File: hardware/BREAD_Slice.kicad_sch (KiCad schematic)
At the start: 15 parts, among them J1 Conn_01x10_Female, J2 I2C_01x04

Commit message: Initial commit
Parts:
- removed C1, C3, C4: 22uF, Capacitor_SMD:C_1206_3216Metric, symbol Device:C_Small
- removed C2: 100nF, Capacitor_SMD:C_1206_3216Metric, symbol Device:C_Small
- removed D1: WS2812B_5050, SparkFun-LED:WS2812-5050-4PIN, symbol SparkFun-LED:WS2812B_5050
- removed HS1: Heatsink_Pad, SparkFun-Fuse:Thermal Pad, symbol Mechanical:Heatsink_Pad
- removed J2: I2C_01x04, Connector_JST:JST_SH_SM04B-SRSS-TB_1x04-1MP_P1.00mm_Horizontal, symbol SparkFun-Connector:I2C_01x04
- removed L1: 4.7uH, Inductor_SMD:L_1210_3225Metric, symbol Device:L_Small
- removed U1: ~, Package_TO_SOT_SMD:TSOT-23-6, symbol SparkFun-DiscreteSemi:AP63205
- added C1, C2: 10uF_t, OCI_UPL_FOOTPRINTS:C_2312, symbol BREAD_Slice-rescue:10uF_t-OCI_UPL_2_Capacitors
- added D1, D2, D3, D4: D, Diode_SMD:D_1206_3216Metric_Pad1.42x1.75mm_HandSolder, symbol Device:D
- added D5, D6, D7, D8: D_Zener, Diode_SMD:D_1206_3216Metric_Pad1.42x1.75mm_HandSolder, symbol Device:D_Zener
- added J2, J3, J4, J5: Screw_Terminal_01x03, TerminalBlock_TE-Connectivity:TerminalBlock_TE_282834-3_1x03_P2.54mm_Horizontal, symbol Connector:Screw_Terminal_01x03
- added J6: Screw_Terminal_01x04, TerminalBlock_TE-Connectivity:TerminalBlock_TE_282834-4_1x04_P2.54mm_Horizontal, symbol Connector:Screw_Terminal_01x04
- added K1, K2, K3, K4: G5Q-1, Relay_THT:Relay_SPDT_Omron-G5Q-1, symbol Relay:G5Q-1
- added Logo1: Logo_Open_Hardware_Small, Symbol:OSHW-Symbol_6.7x6mm_SilkScreen, symbol Graphic:Logo_Open_Hardware_Small
- added R1, R2, R3, R4: 1k, Resistor_SMD:R_1206_3216Metric_Pad1.30x1.75mm_HandSolder, symbol BREAD_Slice-rescue:R-OCI_UPL_1_Resistors
- added RV1, RV2, RV3, RV4: 10k, Potentiometer_THT:Potentiometer_Bourns_3266W_Vertical, symbol BREAD_Slice-rescue:R_POT_TRIM-Device
- added U1, U2, U3, U4: TCMT1100, Package_SO:SOP-4_4.4x2.6mm_P1.27mm, symbol Isolator:TCMT1100
- H1, H4: footprint MountingHole:MountingHole_5mm -> MountingHole:MountingHole_3.2mm_M3_DIN965_Pad
- H2: renamed from H3; footprint MountingHole:MountingHole_5mm -> MountingHole:MountingHole_3.2mm_M3_DIN965_Pad
- H3: renamed from H2; footprint MountingHole:MountingHole_5mm -> MountingHole:MountingHole_3.2mm_M3_DIN965_Pad
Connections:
- net +12V: now also A1.30 (VIN), C1.1
- net +5V: now also C2.1, D1.1 (K), D2.1 (K), D3.1 (K), D4.1 (K), K1.5, K2.5, K3.5, K4.5
- net GND: now also C1.2, C2.2, D5.1 (K), D5.2 (A), D6.1 (K), D6.2 (A), D7.1 (K), D7.2 (A), D8.1 (K), D8.2 (A), RV1.3, RV2.3, RV3.3, RV4.3, U1.2, U1.3, U2.2, U2.3, U3.2, U3.3, U4.2, U4.3
- net SW2: now reaches A1.12 (D9)
- net SW2: now also R3.1
- net SW3: now reaches A1.13 (D10)
- net SW3: now also R2.1
- net SW4: now reaches A1.14 (D11)
- net SW4: now also R4.1
- net A_IN1: now reaches A1.19 (A0)
- net A_IN1: now also RV1.2
- net A_IN2: now reaches A1.20 (A1)
- net A_IN2: now also RV2.2
- net A_IN3: now reaches A1.21 (A2)
- net A_IN3: now also RV3.2
- net A_IN4: now reaches A1.22 (A3)
- net A_IN4: now also RV4.2
- net SW1: now reaches A1.9 (D6)
- net SW1: now also R1.1
- net LED: no longer names the net of A1.8 (D5)
- new net: D1.2 (A), K1.1, U1.4
- new net: R1.2, U1.1
- new net: J2.1 (Pin_1), K1.4
- new net: J2.2 (Pin_2), K1.3
- new net: J2.3 (Pin_3), K1.2
- new net: D2.2 (A), K3.1, U2.4
- new net: R2.2, U2.1
- new net: J3.1 (Pin_1), K3.4
- new net: J3.2 (Pin_2), K3.3
- new net: J3.3 (Pin_3), K3.2
- new net: D3.2 (A), K2.1, U3.4
- new net: R3.2, U3.1
- new net: J4.1 (Pin_1), K2.4
- new net: J4.2 (Pin_2), K2.3
- new net: J4.3 (Pin_3), K2.2
- new net: D4.2 (A), K4.1, U4.4
- new net: R4.2, U4.1
- new net: J5.1 (Pin_1), K4.4
- new net: J5.2 (Pin_2), K4.3
- new net: J5.3 (Pin_3), K4.2
- new net F_1: J6.1 (Pin_1), RV1.1
- new net F_2: J6.2 (Pin_2), RV2.1
- new net F_3: J6.3 (Pin_3), RV3.1
- new net F_4: J6.4 (Pin_4), RV4.1
- no-connect marks 22 -> 6
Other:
- note added: "NC NO IN"
- moved on the sheet: A1, H1, H2, H3, H4, J1

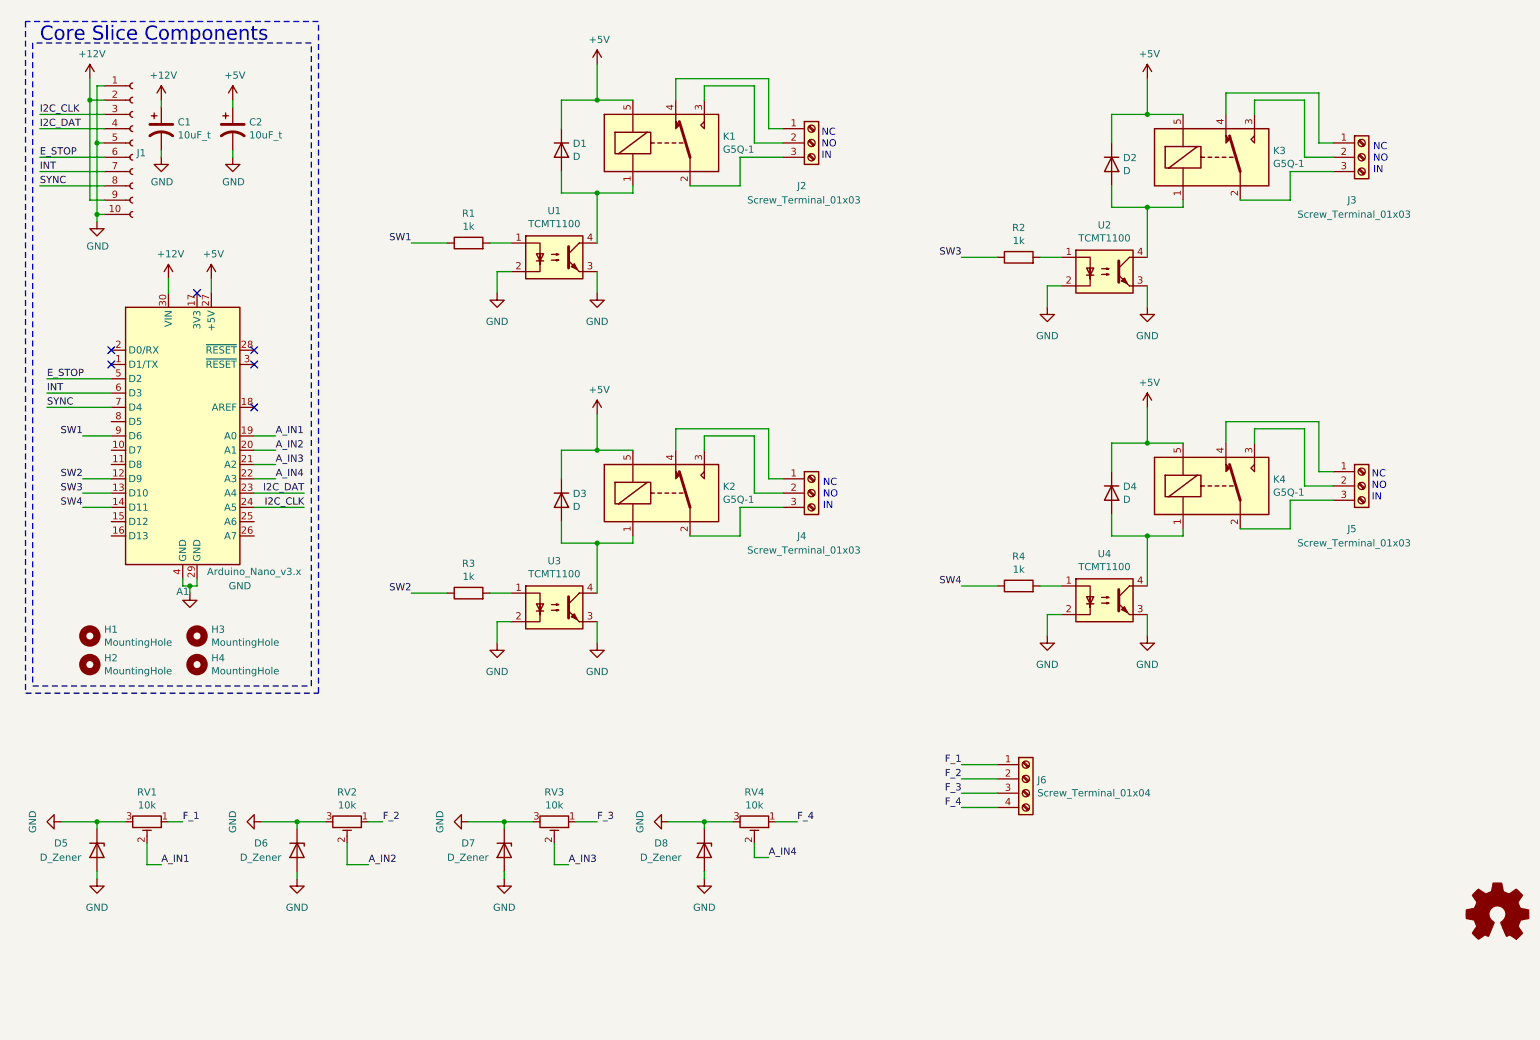
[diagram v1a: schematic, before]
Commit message: added firmware and the updated PCB with new BREAD format
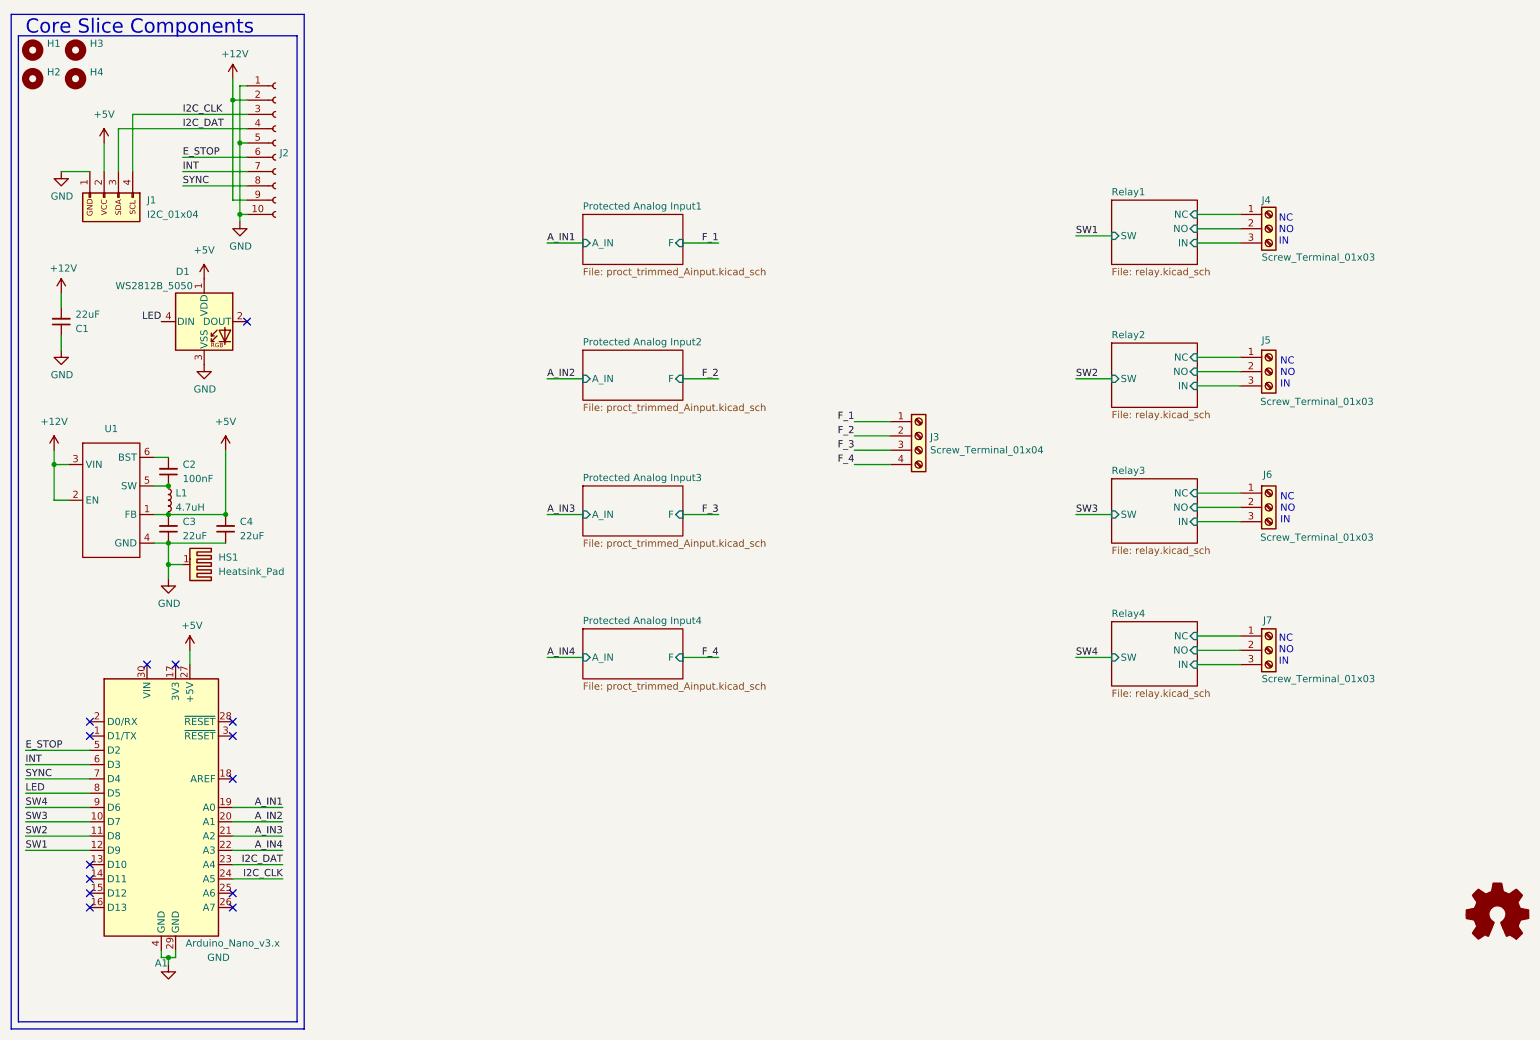
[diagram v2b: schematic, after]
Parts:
- removed C1, C2: 10uF_t, OCI_UPL_FOOTPRINTS:C_2312, symbol BREAD_Slice-rescue:10uF_t-OCI_UPL_2_Capacitors
- removed D1, D2, D3, D4: D, Diode_SMD:D_1206_3216Metric_Pad1.42x1.75mm_HandSolder, symbol Device:D
- removed D5, D6, D7, D8: D_Zener, Diode_SMD:D_1206_3216Metric_Pad1.42x1.75mm_HandSolder, symbol Device:D_Zener
- removed J2, J3: Screw_Terminal_01x03, TerminalBlock_TE-Connectivity:TerminalBlock_TE_282834-3_1x03_P2.54mm_Horizontal, symbol Connector:Screw_Terminal_01x03
- removed J6: Screw_Terminal_01x04, TerminalBlock_TE-Connectivity:TerminalBlock_TE_282834-4_1x04_P2.54mm_Horizontal, symbol Connector:Screw_Terminal_01x04
- removed K1, K2, K3, K4: G5Q-1, Relay_THT:Relay_SPDT_Omron-G5Q-1, symbol Relay:G5Q-1
- removed Logo1: Logo_Open_Hardware_Small, Symbol:OSHW-Symbol_6.7x6mm_SilkScreen, symbol Graphic:Logo_Open_Hardware_Small
- removed R1, R2, R3, R4: 1k, Resistor_SMD:R_1206_3216Metric_Pad1.30x1.75mm_HandSolder, symbol BREAD_Slice-rescue:R-OCI_UPL_1_Resistors
- removed RV1, RV2, RV3, RV4: 10k, Potentiometer_THT:Potentiometer_Bourns_3266W_Vertical, symbol BREAD_Slice-rescue:R_POT_TRIM-Device
- removed U1, U2, U3, U4: TCMT1100, Package_SO:SOP-4_4.4x2.6mm_P1.27mm, symbol Isolator:TCMT1100
- added C1, C3, C4: 22uF, Capacitor_SMD:C_1206_3216Metric, symbol Device:C_Small
- added C2: 100nF, Capacitor_SMD:C_1206_3216Metric, symbol Device:C_Small
- added D1: WS2812B_5050, SparkFun-LED:WS2812-5050-4PIN, symbol SparkFun-LED:WS2812B_5050
- added HS1: Heatsink_Pad, KML-Custom:Thermal Pad, symbol Mechanical:Heatsink_Pad
- added J1: I2C_01x04, Connector_JST:JST_SH_SM04B-SRSS-TB_1x04-1MP_P1.00mm_Horizontal, symbol SparkFun-Connector:I2C_01x04
- added J3: Screw_Terminal_01x04, TerminalBlock_TE-Connectivity:TerminalBlock_TE_282834-4_1x04_P2.54mm_Horizontal, symbol Connector:Screw_Terminal_01x04
- added J6, J7: Screw_Terminal_01x03, TerminalBlock_TE-Connectivity:TerminalBlock_TE_282834-3_1x03_P2.54mm_Horizontal, symbol Connector:Screw_Terminal_01x03
- added L1: 4.7uH, Inductor_SMD:L_1210_3225Metric, symbol Device:L_Small
- added U1: ~, Package_TO_SOT_SMD:TSOT-23-6, symbol SparkFun-DiscreteSemi:AP63205
- H1, H4: footprint MountingHole:MountingHole_3.2mm_M3_DIN965_Pad -> MountingHole:MountingHole_5mm
- H2: renamed from H3; footprint MountingHole:MountingHole_3.2mm_M3_DIN965_Pad -> MountingHole:MountingHole_5mm
- H3: renamed from H2; footprint MountingHole:MountingHole_3.2mm_M3_DIN965_Pad -> MountingHole:MountingHole_5mm
- renumbered J1 to J2
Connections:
- net +12V: now also C1.2, U1.2 (EN), U1.3 (VIN); no longer A1.30 (VIN)
- net +5V: now also C3.2, C4.2, D1.1 (VDD), J1.2 (Pin_2), L1.2, U1.1 (FB)
- net F_1: now also J3.1 (Pin_1)
- net F_2: now also J3.2 (Pin_2)
- net F_3: now also J3.3 (Pin_3)
- net F_4: now also J3.4 (Pin_4)
- net GND: now also C1.1, C3.1, C4.1, D1.3 (VSS), HS1.1, J1.1 (Pin_1), U1.4 (GND)
- net I2C_CLK: now also J1.4 (Pin_4)
- net I2C_DAT: now also J1.3 (Pin_3)
- net SW1: now also A1.12 (D9); no longer A1.9 (D6)
- net SW2: now also A1.11 (D8); no longer A1.12 (D9)
- net SW3: now also A1.10 (D7); no longer A1.13 (D10)
- net SW4: now also A1.9 (D6); no longer A1.14 (D11)
- net LED: now reaches A1.8 (D5)
- net LED: now also D1.4 (DIN)
- net Relay1/NC: now reaches J4.1 (Pin_1)
- net Relay1/NO: now reaches J4.2 (Pin_2)
- net Relay1/IN: now reaches J4.3 (Pin_3)
- net Relay2/NC: now reaches J5.1 (Pin_1)
- net Relay2/NO: now reaches J5.2 (Pin_2)
- net Relay2/IN: now reaches J5.3 (Pin_3)
- new net: C2.1, L1.1, U1.5 (SW)
- new net: C2.2, U1.6 (BST)
- new net Relay3/IN: J6.3 (Pin_3)
- new net Relay3/NC: J6.1 (Pin_1)
- new net Relay3/NO: J6.2 (Pin_2)
- new net Relay4/IN: J7.3 (Pin_3)
- new net Relay4/NC: J7.1 (Pin_1)
- new net Relay4/NO: J7.2 (Pin_2)
- no-connect marks 6 -> 14
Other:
- added sheet Protected Analog Input1 (proct_trimmed_Ainput.kicad_sch)
- added sheet Protected Analog Input2 (proct_trimmed_Ainput.kicad_sch)
- added sheet Protected Analog Input3 (proct_trimmed_Ainput.kicad_sch)
- added sheet Protected Analog Input4 (proct_trimmed_Ainput.kicad_sch)
- added sheet Relay1 (relay.kicad_sch)
- added sheet Relay2 (relay.kicad_sch)
- added sheet Relay3 (relay.kicad_sch)
- added sheet Relay4 (relay.kicad_sch)
- moved on the sheet: A1, H1, H2, H3, H4, J2

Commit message: changed terminals to meet those of the relays max output with margin
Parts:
- J3: footprint TerminalBlock_TE-Connectivity:TerminalBlock_TE_282834-4_1x04_P2.54mm_Horizontal -> TerminalBlock_Phoenix:TerminalBlock_Phoenix_MPT-0,5-4-2.54_1x04_P2.54mm_Horizontal
- J4, J5, J6, J7: footprint TerminalBlock_TE-Connectivity:TerminalBlock_TE_282834-3_1x03_P2.54mm_Horizontal -> TerminalBlock_Phoenix:TerminalBlock_Phoenix_MKDS-1,5-3-5.08_1x03_P5.08mm_Horizontal
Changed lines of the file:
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@@
 			)
 		)
-		(property "Footprint" "TerminalBlock_TE-Connectivity:TerminalBlock_TE_282834-3_1x03_P2.54mm_Horizontal"
+		(property "Footprint" "TerminalBlock_Phoenix:TerminalBlock_Phoenix_MKDS-1,5-3-5.08_1x03_P5.08mm_Horizontal"
 			(at 237.49 101.6 0)
 			(effects
@@
 			)
 		)
-		(property "Footprint" "TerminalBlock_TE-Connectivity:TerminalBlock_TE_282834-3_1x03_P2.54mm_Horizontal"
+		(property "Footprint" "TerminalBlock_Phoenix:TerminalBlock_Phoenix_MKDS-1,5-3-5.08_1x03_P5.08mm_Horizontal"
 			(at 237.49 127 0)
 			(effects
@@
 			)
 		)
-		(property "Footprint" "TerminalBlock_TE-Connectivity:TerminalBlock_TE_282834-4_1x04_P2.54mm_Horizontal"
+		(property "Footprint" "TerminalBlock_Phoenix:TerminalBlock_Phoenix_MPT-0,5-4-2.54_1x04_P2.54mm_Horizontal"
 			(at 175.26 88.9 0)
 			(effects
@@
 			)
 		)
-		(property "Footprint" "TerminalBlock_TE-Connectivity:TerminalBlock_TE_282834-3_1x03_P2.54mm_Horizontal"
+		(property "Footprint" "TerminalBlock_Phoenix:TerminalBlock_Phoenix_MKDS-1,5-3-5.08_1x03_P5.08mm_Horizontal"
 			(at 237.49 52.07 0)
 			(effects
@@
 			)
 		)
-		(property "Footprint" "TerminalBlock_TE-Connectivity:TerminalBlock_TE_282834-3_1x03_P2.54mm_Horizontal"
+		(property "Footprint" "TerminalBlock_Phoenix:TerminalBlock_Phoenix_MKDS-1,5-3-5.08_1x03_P5.08mm_Horizontal"
 			(at 237.49 77.47 0)
 			(effects
